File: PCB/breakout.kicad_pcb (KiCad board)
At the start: 2 copper layers, 22.8 x 17.8 mm, 14 parts, among them J1 BKOUT_PINS, J2 POTENTIOMETER, U1 AD5293

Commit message: rev 0.0.0 final
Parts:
- added D3: SD0805, Diode_SMD:D_0805_2012Metric, F.Cu at (156.7, 103.1)
- added D4: SD0805, Diode_SMD:D_0805_2012Metric, F.Cu at (141.6, 101.9)
- moved G*** 6.47 mm to (148.4, 105.4)
- moved D1 3.63 mm to (138.7, 102.6), turned to -90 degrees
- moved C4 3.44 mm to (156.7, 107.3)
- moved C5 3.44 mm to (156.7, 105.3)
- moved R1 3.03 mm to (138.7, 106.2), turned to 90 degrees
- moved C3 2.03 mm to (141.6, 105.9)
- moved C2 2.03 mm to (141.6, 103.9)
- moved C6 0.13 mm to (141.6, 111.3)
- moved C7 0.13 mm to (141.6, 109.2)
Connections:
- J2 pad 1: /Vdd+ -> Net-(J2-Pad1)
- J2 pad 5: /Vss- -> Net-(J2-Pad5)
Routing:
- net Net-(J2-Pad5): track 0.00 -> 9.40 mm
- net /Vcc: track 24.3 -> 29.4 mm, vias 2 -> 1
- net Net-(D1-Pad2): track 5.35 -> 1.71 mm
- net /Vdd+: track 10.7 -> 7.30 mm
- net Net-(J2-Pad1): track 0.00 -> 3.35 mm
- net /Vss-: track 21.8 -> 21.3 mm, vias 1 -> 2
- net GND: vias 13 -> 14

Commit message: initial repo load
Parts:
- turned D3 to 180 degrees
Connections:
- D3 pad 1: /Vss- -> Net-(J2-Pad5)
- D3 pad 2: Net-(J2-Pad5) -> /Vss-
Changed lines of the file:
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@@
   (net 15 "Net-(D1-Pad2)")
   (net 16 "Net-(J2-Pad5)")
-  (net 17 "Net-(J2-Pad1)")
+  (net 17 "Net-(D4-Pad2)")
   (footprint "LED_SMD:LED_0805_2012Metric" (layer "F.Cu")
     (at 138.684 102.616 -90)
@@
   )
   (footprint "Diode_SMD:D_0805_2012Metric" (layer "F.Cu")
-    (at 156.718 103.124)
+    (at 156.718 103.124 180)
     (descr "Diode SMD 0805 (2012 Metric), square (rectangular) end terminal, IPC_7351 nominal, (Body size source: https://docs.google.com/spreadsheets/d/1BsfQQcO9C6DZCsRaXUlFlo91Tg2WpOkGARC1WS5S8t0/edit?usp=sharing), generated with kicad-footprint-generator")
     (tags "diode")
@@
     (property "Sheetname" "")
     (attr smd)
-    (fp_text reference "D3" (at -2.032 -1.397) (layer "F.SilkS")
-      (effects (font (size 0.5 0.5) (thickness 0.1)))
-    )
-    (fp_text value "SD0805" (at 0.889 -1.397 180) (layer "F.SilkS")
+    (fp_text reference "D3" (at 1.905 1.397) (layer "F.SilkS")
+      (effects (font (size 0.5 0.5) (thickness 0.1)))
+    )
+    (fp_text value "SD0805" (at -0.762 1.397) (layer "F.SilkS")
       (effects (font (size 0.5 0.5) (thickness 0.1)))
     )
@@
     (fp_line (start 1 0.6) (end 1 -0.6) (layer "F.Fab") (width 0.1))
     (fp_line (start -1 0.6) (end 1 0.6) (layer "F.Fab") (width 0.1))
-    (pad "1" smd roundrect (at -0.9375 0) (size 0.975 1.4) (layers "F.Cu" "F.Paste" "F.Mask") (roundrect_rratio 0.25)
-      (net 4 "/Vss-") (pinfunction "K") (pintype "passive"))
-    (pad "2" smd roundrect (at 0.9375 0) (size 0.975 1.4) (layers "F.Cu" "F.Paste" "F.Mask") (roundrect_rratio 0.25)
-      (net 16 "Net-(J2-Pad5)") (pinfunction "A") (pintype "passive"))
+    (pad "1" smd roundrect (at -0.9375 0 180) (size 0.975 1.4) (layers "F.Cu" "F.Paste" "F.Mask") (roundrect_rratio 0.25)
+      (net 16 "Net-(J2-Pad5)") (pinfunction "K") (pintype "passive"))
+    (pad "2" smd roundrect (at 0.9375 0 180) (size 0.975 1.4) (layers "F.Cu" "F.Paste" "F.Mask") (roundrect_rratio 0.25)
+      (net 4 "/Vss-") (pinfunction "A") (pintype "passive"))
     (model "${KICAD6_3DMODEL_DIR}/Diode_SMD.3dshapes/D_0805_2012Metric.wrl"
       (offset (xyz 0 0 0))
@@
       (net 7 "/Vdd+") (pinfunction "K") (pintype "passive"))
     (pad "2" smd roundrect (at 0.9375 0 180) (size 0.975 1.4) (layers "F.Cu" "F.Paste" "F.Mask") (roundrect_rratio 0.25)
-      (net 17 "Net-(J2-Pad1)") (pinfunction "A") (pintype "passive"))
+      (net 17 "Net-(D4-Pad2)") (pinfunction "A") (pintype "passive"))
     (model "${KICAD6_3DMODEL_DIR}/Diode_SMD.3dshapes/D_0805_2012Metric.wrl"
       (offset (xyz 0 0 0))
@@
     (fp_line (start 1.75 14.45) (end -1.8 14.45) (layer "F.CrtYd") (width 0.05))
     (pad "1" thru_hole circle (at 0 0 90) (size 1.7 1.7) (drill 1) (layers *.Cu *.Mask)
-      (net 17 "Net-(J2-Pad1)") (pinfunction "Pin_1") (pintype "passive"))
+      (net 17 "Net-(D4-Pad2)") (pinfunction "Pin_1") (pintype "passive"))
     (pad "2" thru_hole oval (at 0 2.54 90) (size 1.7 1.7) (drill 1) (layers *.Cu *.Mask)
       (net 5 "/H") (pinfunction "Pin_2") (pintype "passive"))
@@
       (effects (font (size 0.5 0.5) (thickness 0.1)))
     )
-    (fp_text value "1uF" (at 0.889 1.27) (layer "F.SilkS")
-      (effects (font (size 0.5 0.5) (thickness 0.1)))
-    )
+    (fp_text value "1uF" (at 0.508 1.27) (layer "F.SilkS")
+      (effects (font (size 0.5 0.5) (thickness 0.1)))
+    )

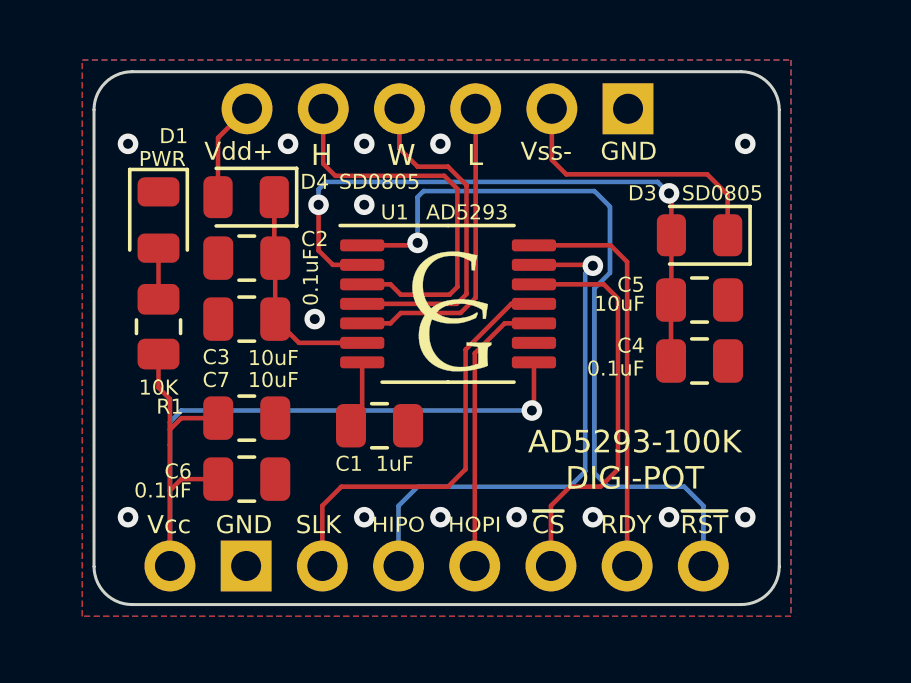
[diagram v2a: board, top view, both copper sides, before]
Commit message: add mounting holes
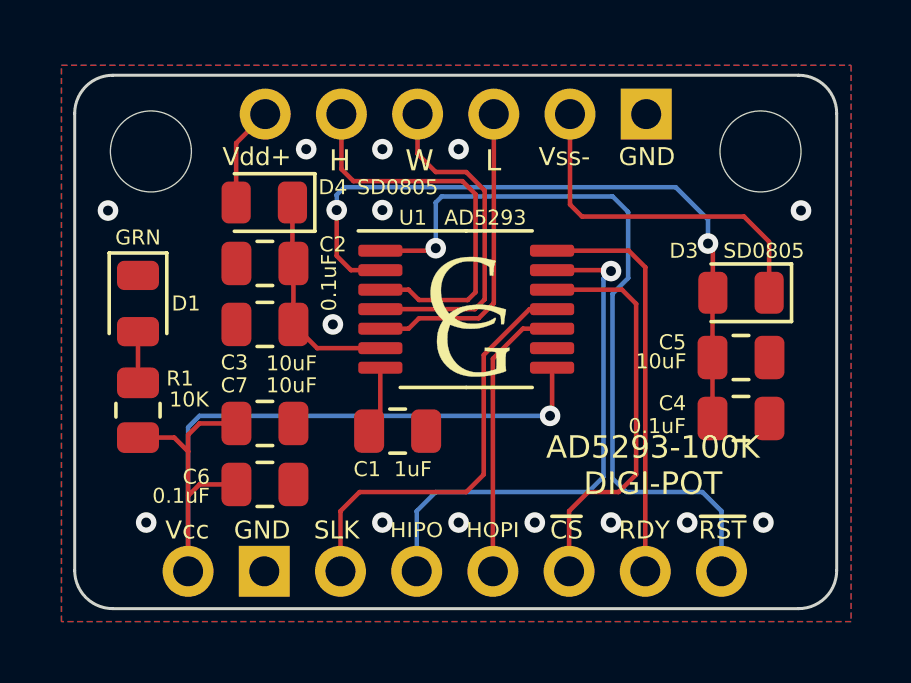
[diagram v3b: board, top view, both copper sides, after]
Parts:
- added REF**: MountingHole_2.7mm_M2.5, MountingHole:MountingHole_2.7mm_M2.5, F.Cu at (158.8, 100.3)
- added REF**: MountingHole_2.7mm_M2.5, MountingHole:MountingHole_2.7mm_M2.5, F.Cu at (138.4, 100.3)
- D1: value PWR -> GRN
- moved D1 2.87 mm to (138.0, 105.4)
- moved R1 2.87 mm to (138.0, 109.0)
- moved C4 2.36 mm to (158.1, 109.2)
- moved C5 2.36 mm to (158.1, 107.2)
- moved D3 2.36 mm to (158.1, 105.0)
- moved C2 0.63 mm to (142.2, 104.1)
- moved C6 0.63 mm to (142.2, 111.4)
- moved C7 0.63 mm to (142.2, 109.4)
- moved D4 0.63 mm to (142.2, 102.0)
- moved J1 0.63 mm to (139.7, 114.3)
- moved J2 0.63 mm to (142.2, 99.1)
- moved C3 0.63 mm to (142.2, 106.1)
- moved G*** 0.63 mm to (149.0, 105.6)
- moved U1 0.63 mm to (148.9, 105.6)
- moved C1 0.63 mm to (146.7, 109.7)
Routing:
- net Net-(D3-Pad1): track 9.40 -> 11.9 mm
- net /Vss-: track 21.3 -> 23.3 mm
- net /Vcc: track 29.4 -> 28.6 mm
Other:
- board size 22.8 x 17.8 mm -> 25.4 x 17.8 mm

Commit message: add mounting holes; version 1.0.0
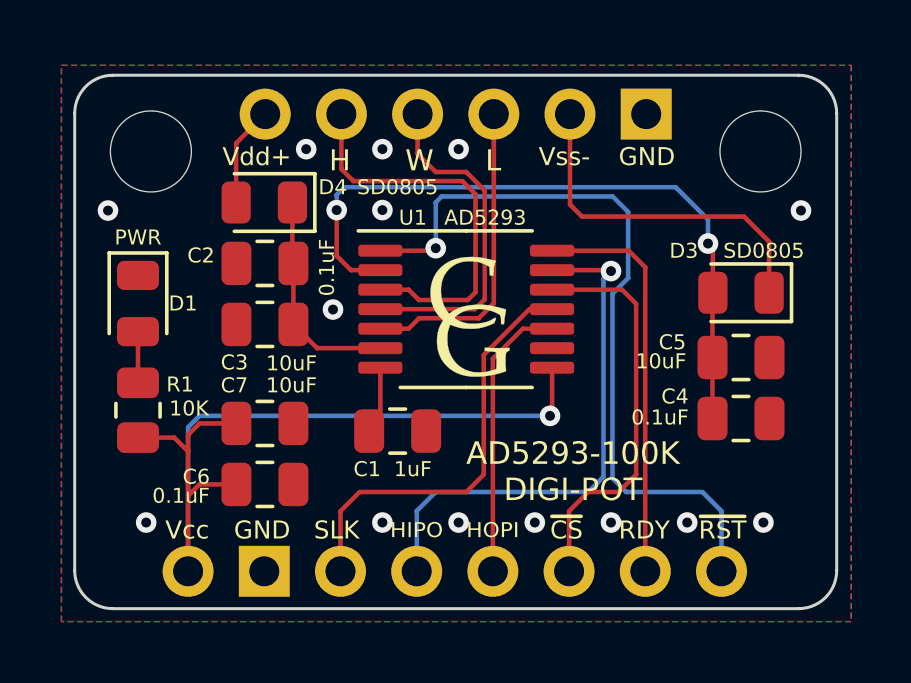
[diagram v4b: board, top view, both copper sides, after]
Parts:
- D1: value GRN -> PWR
- moved G*** 2.83 mm to (145.1, 104.7)
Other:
- board text added: "2023-02-05 1.0.0"
- board text removed: "2023-02-04 0.0.0"
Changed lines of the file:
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@@
     (title "AD5293_breakout")
     (date "2023-02-05")
-    (rev "0.0.0")
+    (rev "1.0.0")
     (company "Cedar Grove Studios")
   )
@@
     (property "Sheetname" "")
     (attr smd)
-    (fp_text reference "D1" (at 0 -1.6 180) (layer "F.SilkS")
+    (fp_text reference "D1" (at 0 -1.5 180) (layer "F.SilkS")
       (effects (font (size 0.5 0.5) (thickness 0.1)))
     )
-    (fp_text value "GRN" (at -2.2 0) (layer "F.SilkS")
+    (fp_text value "PWR" (at -2.2 0) (layer "F.SilkS")
       (effects (font (size 0.5 0.5) (thickness 0.1)))
     )
@@
     (property "Sheetname" "")
     (attr smd)
-    (fp_text reference "C2" (at -2.266 0.635) (layer "F.SilkS")
+    (fp_text reference "C2" (at 2.1298 0.2638) (layer "F.SilkS")
       (effects (font (size 0.5 0.5) (thickness 0.1)))
     )
-    (fp_text value "0.1uF" (at -2.139 -0.635 90) (layer "F.SilkS")
+    (fp_text value "0.1uF" (at -2.0702 -0.1362 90) (layer "F.SilkS")
       (effects (font (size 0.5 0.5) (thickness 0.1)))
     )
@@
     (property "Sheetname" "")
     (attr smd)
-    (fp_text reference "R1" (at 1.056 1.4) (layer "F.SilkS")
+    (fp_text reference "R1" (at 0.856 1.4) (layer "F.SilkS")
       (effects (font (size 0.5 0.5) (thickness 0.1)))
     )
-    (fp_text value "10K" (at 0.356 1.7) (layer "F.SilkS")
+    (fp_text value "10K" (at 0.056 1.7) (layer "F.SilkS")
       (effects (font (size 0.5 0.5) (thickness 0.1)))
     )
@@
     (property "Sheetname" "")
     (attr smd)
-    (fp_text reference "C4" (at -2.286 -0.508) (layer "F.SilkS")
+    (fp_text reference "C4" (at -2.2 -0.732) (layer "F.SilkS")
       (effects (font (size 0.5 0.5) (thickness 0.1)))
     )
-    (fp_text value "0.1uF" (at -2.794 0.254) (layer "F.SilkS")
+    (fp_text value "0.1uF" (at -2.7 -0.032) (layer "F.SilkS")
       (effects (font (size 0.5 0.5) (thickness 0.1)))
     )
@@
   )
   (footprint "CedarGrove_custom:CedarGroveStudios_TEXT_LOGO_8x5_4mm" (layer "B.Cu")
-    (at 142.494 105.791 180)
+    (at 145.1 104.7 180)
     (attr through_hole board_only)
     (fp_text reference "G***" (at 0 -3.1) (layer "B.Fab") hide
@@
     (effects (font (size 0.6 0.6) (thickness 0.1)) (justify mirror))
   )
-  (gr_text "AD5293 - 100K\nDigital Potentiometer" (at 152.654 105.791) (layer "B.SilkS")
+  (gr_text "AD5293 - 100K\nDigital Potentiometer" (at 153.9 105.9) (layer "B.SilkS")
     (effects (font (size 0.6 0.6) (thickness 0.1)) (justify mirror))
   )
-  (gr_text "2023-02-04 0.0.0" (at 152.527 107.569) (layer "B.SilkS")
+  (gr_text "2023-02-05 1.0.0" (at 153.7 107.5) (layer "B.SilkS")
     (effects (font (size 0.5 0.5) (thickness 0.1)) (justify mirror))
   )
-  (gr_text "AD5293-100K\nDIGI-POT" (at 155.1638 110.7948) (layer "F.SilkS")
+  (gr_text "AD5293-100K\nDIGI-POT" (at 152.5 111) (layer "F.SilkS")
     (effects (font (size 0.75 0.75) (thickness 0.15)))
   )
@@
   (via (at 146.1468 112.6998) (size 0.6858) (drill 0.3302) (layers "F.Cu" "B.Cu") (net 1))
   (via (at 146.1468 102.2858) (size 0.6858) (drill 0.3302) (layers "F.Cu" "B.Cu") (net 1))
-  (via (at 144.4958 106.0958) (size 0.6858) (drill 0.3302) (layers "F.Cu" "B.Cu") (net 1))
+  (via (at 144.5 105.6) (size 0.6858) (drill 0.3302) (layers "F.Cu" "B.Cu") (net 1))
   (via (at 138.2728 112.6998) (size 0.6858) (drill 0.3302) (layers "F.Cu" "B.Cu") (net 1))
   (via (at 148.6868 112.6998) (size 0.6858) (drill 0.3302) (layers "F.Cu" "B.Cu") (net 1))

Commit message: refactor layout design; simplify routing
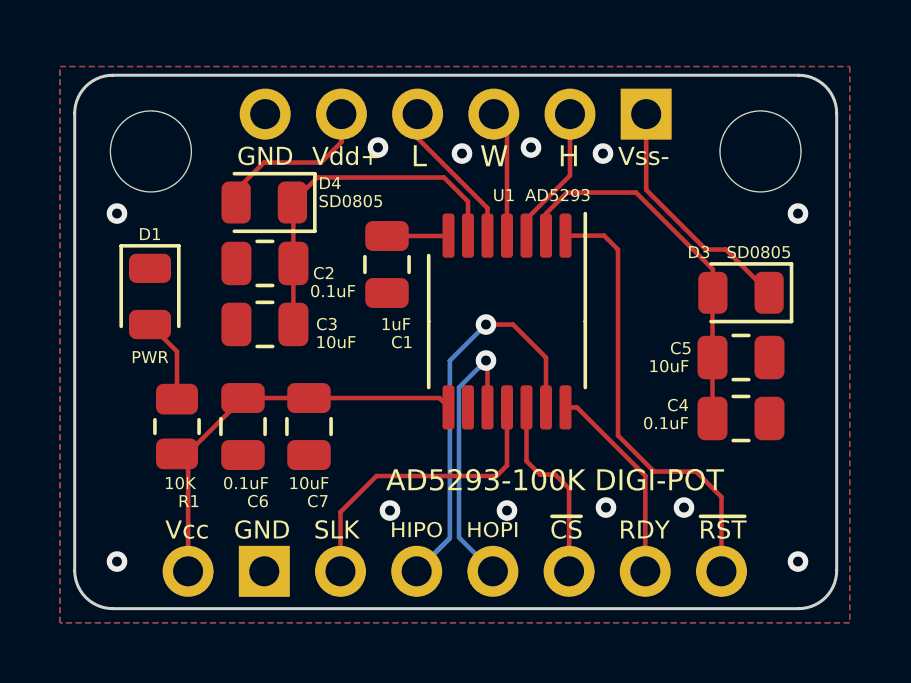
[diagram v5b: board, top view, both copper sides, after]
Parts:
- removed the G*** at (149.0, 105.6)
- moved C1 5.56 mm to (146.3, 104.1), turned to -90 degrees
- moved G*** 2.18 mm to (143.0, 104.1)
- moved C6 2.06 mm to (141.5, 109.5), turned to -90 degrees
- moved C7 1.47 mm to (143.7, 109.5), turned to -90 degrees
- moved U1 1.42 mm to (150.3, 106.0), turned to -90 degrees
- moved R1 1.41 mm to (139.3, 109.5)
- moved D1 0.47 mm to (138.4, 105.2)
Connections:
- J2 pad 1: Net-(D4-Pad2) -> GND
- J2 pad 2: /H -> Net-(D4-Pad2)
- J2 pad 3: /W -> /L
- J2 pad 4: /L -> /W
- J2 pad 5: Net-(D3-Pad1) -> /H
- J2 pad 6: GND -> Net-(D3-Pad1)
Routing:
- net /Vcc: track 28.6 -> 14.0 mm, vias 1 -> 0
- net /Vss-: track 23.3 -> 12.6 mm, vias 2 -> 0
- net /~{RST}: track 25.3 -> 14.9 mm, vias 1 -> 0
- net /H: track 13.3 -> 4.65 mm
- net /~{CS}: track 13.4 -> 6.34 mm
- net /W: track 11.3 -> 4.23 mm
- net /RDY: track 13.5 -> 6.79 mm
- net /L: track 10.4 -> 5.02 mm
- net /Vdd+: track 7.30 -> 11.7 mm
- net /HIPO: track 17.6 -> 13.3 mm
- net /SCK: track 14.2 -> 10.1 mm
- net Net-(D3-Pad1): track 11.9 -> 8.04 mm
- net Net-(D4-Pad2): track 3.35 -> 5.51 mm
- net Net-(D1-Pad2): track 1.71 -> 2.86 mm
- net /HOPI: track 9.48 -> 9.45 mm, vias 0 -> 1
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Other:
- board text added: "2023-02-08 1.0.1"
- board text removed: "2023-02-05 1.0.0"

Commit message: update to ver 2.0.0
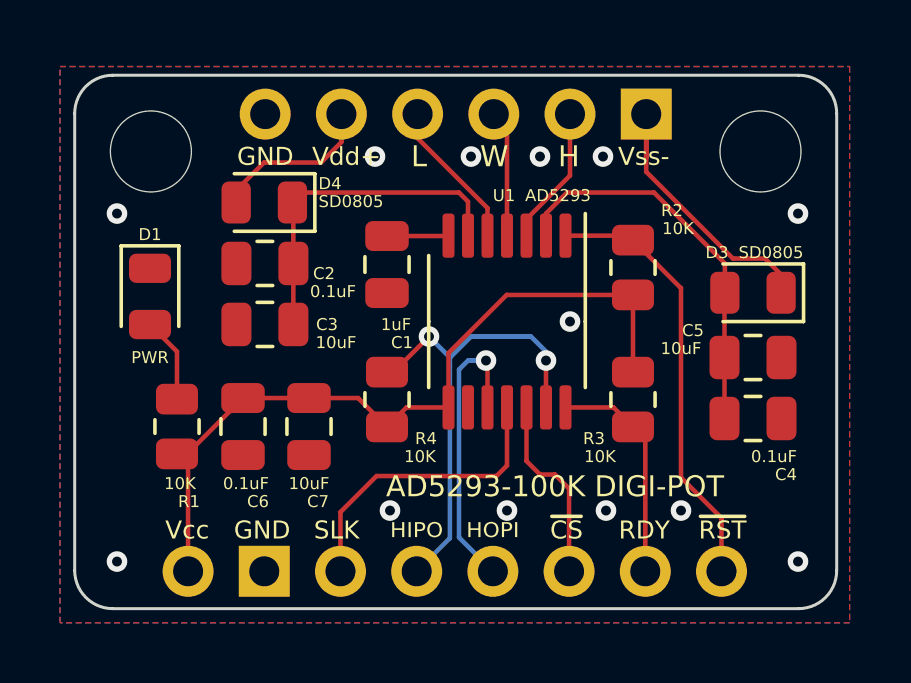
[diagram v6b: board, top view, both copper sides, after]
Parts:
- added R2: 10K, Resistor_SMD:R_0805_2012Metric, F.Cu at (154.5, 104.2)
- added R3: 10K, Resistor_SMD:R_0805_2012Metric, F.Cu at (154.5, 108.6)
- added R4: 10K, Resistor_SMD:R_0805_2012Metric, F.Cu at (146.3, 108.6)
- moved C4 0.40 mm to (158.5, 109.2)
- moved C5 0.40 mm to (158.5, 107.2)
- moved D3 0.40 mm to (158.5, 105.0)
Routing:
- net /Vcc: track 14.0 -> 25.9 mm
- net /HIPO: track 13.3 -> 16.2 mm, vias 1 -> 2
- net Net-(D3-Pad1): track 8.04 -> 9.92 mm
- net /RDY: track 6.79 -> 7.50 mm
- net /Vss-: track 12.6 -> 13.1 mm
- net GND: vias 12 -> 13
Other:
- board text added: "2023-03-17 2.0.0"
- board text removed: "2023-02-08 1.0.1"

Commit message: update PCB design
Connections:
- net /HIPO renamed /SDO
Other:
- board text added: "2023-03-25 2.0.1"
- board text added: "SDO"
- board text removed: "2023-03-17 2.0.0"
- board text removed: "HIPO"
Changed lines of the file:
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@@
   (title_block
     (title "AD5293_breakout")
-    (date "2023-03-17")
-    (rev "2.0.0")
+    (date "2023-03-25")
+    (rev "2.0.1")
     (company "Cedar Grove Studios")
   )
@@
   (net 10 "/SCK")
   (net 11 "/~{CS}")
-  (net 12 "/HIPO")
+  (net 12 "/SDO")
   (net 13 "/RDY")
   (net 14 "/Vcc")
@@
       (net 10 "/SCK") (pinfunction "Pin_3") (pintype "passive"))
     (pad "4" thru_hole oval (at 0 7.62 90) (size 1.7 1.7) (drill 1) (layers *.Cu *.Mask)
-      (net 12 "/HIPO") (pinfunction "Pin_4") (pintype "passive"))
+      (net 12 "/SDO") (pinfunction "Pin_4") (pintype "passive"))
     (pad "5" thru_hole oval (at 0 10.16 90) (size 1.7 1.7) (drill 1) (layers *.Cu *.Mask)
       (net 9 "/HOPI") (pinfunction "Pin_5") (pintype "passive"))
@@
       (net 11 "/~{CS}") (pinfunction "~{CS}") (pintype "input"))
     (pad "13" smd roundrect (at 2.8625 -1.3 270) (size 1.475 0.4) (layers "F.Cu" "F.Paste" "F.Mask") (roundrect_rratio 0.25)
-      (net 12 "/HIPO") (pinfunction "SDO") (pintype "output"))
+      (net 12 "/SDO") (pinfunction "SDO") (pintype "output"))
     (pad "14" smd roundrect (at 2.8625 -1.95 270) (size 1.475 0.4) (layers "F.Cu" "F.Paste" "F.Mask") (roundrect_rratio 0.25)
       (net 13 "/RDY") (pinfunction "RDY") (pintype "open_collector"))
@@
       (net 14 "/Vcc") (pintype "passive"))
     (pad "2" smd roundrect (at 0.9125 0 90) (size 1.025 1.4) (layers "F.Cu" "F.Paste" "F.Mask") (roundrect_rratio 0.243902439)
-      (net 12 "/HIPO") (pintype "passive"))
+      (net 12 "/SDO") (pintype "passive"))
     (model "${KICAD6_3DMODEL_DIR}/Resistor_SMD.3dshapes/R_0805_2012Metric.wrl"
       (offset (xyz 0 0 0))
@@
     (effects (font (size 0.6 0.6) (thickness 0.1)) (justify mirror))
   )
-  (gr_text "2023-03-17 2.0.0" (at 154.1 106) (layer "B.SilkS")
+  (gr_text "2023-03-25 2.0.1" (at 154.1 106) (layer "B.SilkS")
     (effects (font (size 0.5 0.5) (thickness 0.1)) (justify mirror))
   )
@@
     (effects (font (size 0.5 0.53) (thickness 0.1)) (justify left))
   )
-  (gr_text "HIPO" (at 146.4008 112.9538) (layer "F.SilkS")
+  (gr_text "SDO" (at 146.4008 112.9538) (layer "F.SilkS")
     (effects (font (size 0.5 0.53) (thickness 0.1)) (justify left))
   )
